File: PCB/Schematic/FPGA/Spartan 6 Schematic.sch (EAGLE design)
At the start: 28 parts, among them IC1 XC6SLX25-FT256

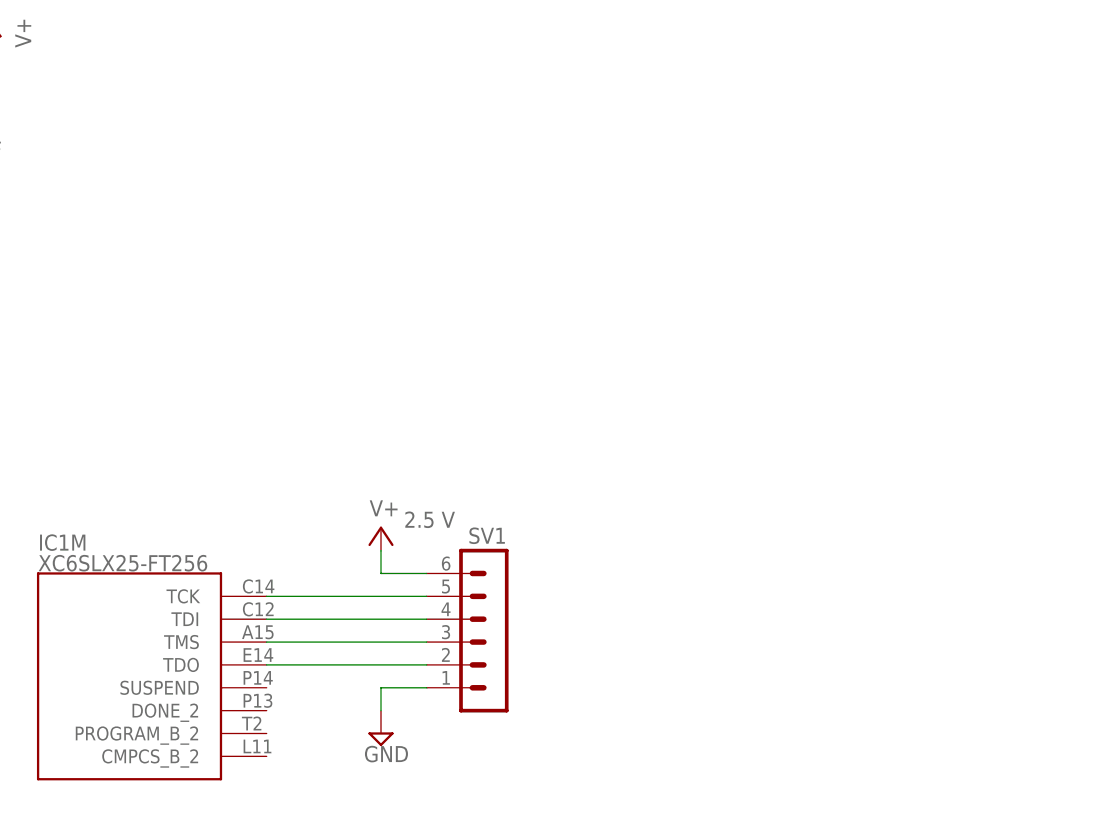
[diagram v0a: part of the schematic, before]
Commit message: FPGA MUX addition
Updated FPGA schematic to include multiplexer for JTAG programming and
added library for Fairchild FST3257MTC multiplexer.
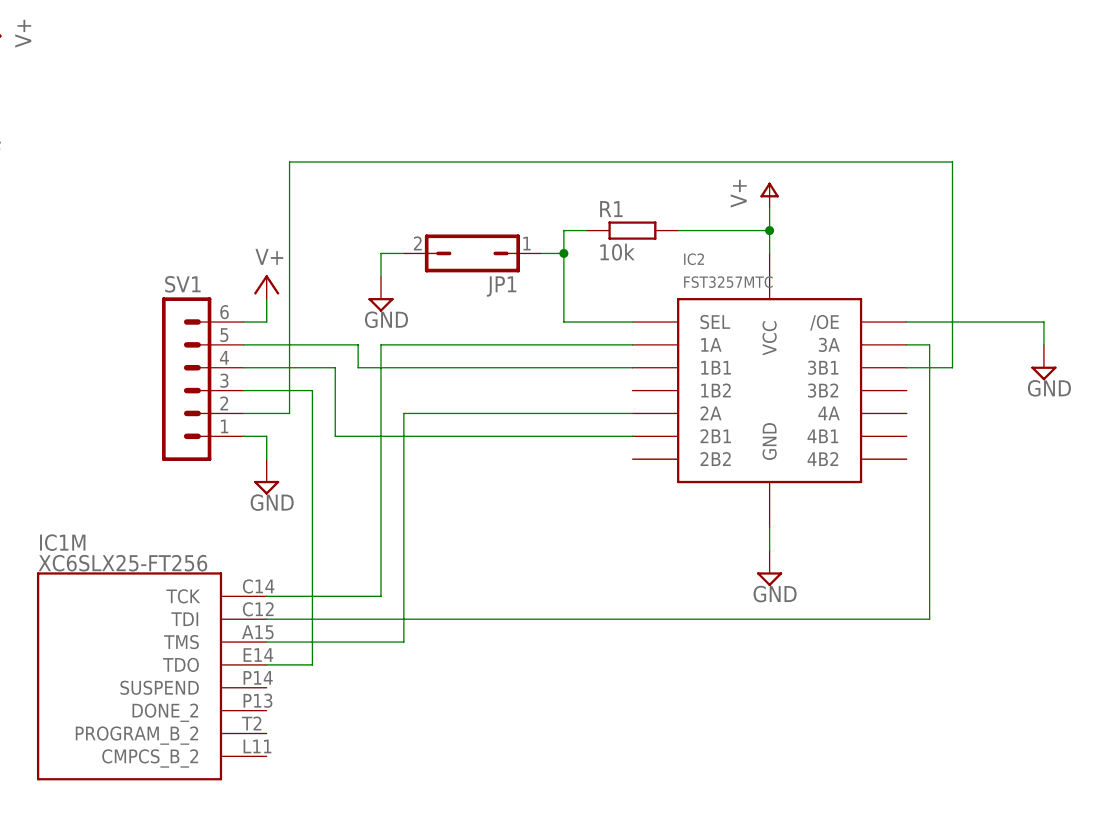
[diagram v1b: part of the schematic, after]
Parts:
- added IC2: FST3257MTC, fairchild_FST3257:FST3257MTC
- added JP1: (no value), jumper:JP1Q
- added R1: 10k, resistor:R-EU_R0805
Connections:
- new net N$5: IC1M.TCK, IC2.1A
- new net N$6: IC1M.TMS, IC2.2A
- new net N$7: IC1M.TDI, IC2.3A
- new net N$8: IC2.SEL, JP1.1, R1.1
- net GND: now also IC2./OE, IC2.GND, JP1.2
- net N$1: now also IC2.1B1; no longer IC1M.TCK
- net N$2: now also IC2.2B1; no longer IC1M.TDI
- net N$3: now also IC1M.TDO; no longer IC1M.TMS
- net N$4: now also IC2.3B1; no longer IC1M.TDO
- net VCCIO_2: now also IC2.VCC, R1.2
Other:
- moved on the sheet: SV1
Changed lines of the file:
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@@
 <part name="P+6" library="supply1" deviceset="V+" device=""/>
 <part name="P+2" library="supply1" deviceset="V+" device=""/>
+<part name="IC2" library="fairchild_FST3257" deviceset="FST3257MTC" device=""/>
+<part name="P+7" library="supply1" deviceset="V+" device=""/>
+<part name="SUPPLY4" library="supply2" deviceset="GND" device=""/>
+<part name="SUPPLY6" library="supply2" deviceset="GND" device=""/>
+<part name="JP1" library="jumper" deviceset="JP1Q" device=""/>
+<part name="R1" library="resistor" deviceset="R-EU_" device="R0805" value="10k"/>
+<part name="SUPPLY9" library="supply2" deviceset="GND" device=""/>
 </parts>
 <sheets>
@@
 <instance part="C26" gate="G$1" x="381" y="96.52"/>
 <instance part="SUPPLY13" gate="GND" x="381" y="88.9"/>
-<instance part="SV1" gate="1" x="474.98" y="17.78" rot="MR0"/>
-<instance part="SUPPLY3" gate="GND" x="462.28" y="5.08"/>
-<instance part="VCCAUX1" gate="1" x="462.28" y="27.94">
-<attribute name="VCCO" x="464.82" y="27.94" size="1.778" layer="96"/>
-</instance>
+<instance part="SV1" gate="1" x="439.42" y="45.72"/>
+<instance part="SUPPLY3" gate="GND" x="449.58" y="33.02"/>
+<instance part="VCCAUX1" gate="1" x="449.58" y="55.88"/>
 <instance part="P+1" gate="1" x="391.16" y="101.6" rot="MR0"/>
 <instance part="P+3" gate="1" x="391.16" y="60.96" rot="MR0"/>
@@
 <instance part="P+6" gate="1" x="391.16" y="15.24" rot="MR0"/>
 <instance part="P+2" gate="1" x="419.1" y="83.82" rot="MR0"/>
+<instance part="IC2" gate="G$1" x="505.46" y="43.18"/>
+<instance part="P+7" gate="1" x="505.46" y="66.04"/>
+<instance part="SUPPLY4" gate="GND" x="505.46" y="22.86"/>
+<instance part="SUPPLY6" gate="GND" x="535.94" y="45.72"/>
+<instance part="JP1" gate="A" x="472.44" y="58.42" rot="R90"/>
+<instance part="R1" gate="G$1" x="490.22" y="60.96"/>
+<instance part="SUPPLY9" gate="GND" x="462.28" y="53.34"/>
 </instances>
 <busses>
@@
 <segment>
 <pinref part="SV1" gate="1" pin="1"/>
-<wire x1="467.36" y1="10.16" x2="462.28" y2="10.16" width="0.1524" layer="91"/>
-<wire x1="462.28" y1="10.16" x2="462.28" y2="7.62" width="0.1524" layer="91"/>
+<wire x1="447.04" y1="38.1" x2="449.58" y2="38.1" width="0.1524" layer="91"/>
+<wire x1="449.58" y1="38.1" x2="449.58" y2="35.56" width="0.1524" layer="91"/>
 <pinref part="SUPPLY3" gate="GND" pin="GND"/>
+</segment>
+<segment>
+<pinref part="SUPPLY4" gate="GND" pin="GND"/>
+<pinref part="IC2" gate="G$1" pin="GND"/>
+<wire x1="505.46" y1="25.4" x2="505.46" y2="27.94" width="0.1524" layer="91"/>
+</segment>
+<segment>
+<pinref part="IC2" gate="G$1" pin="/OE"/>
+<pinref part="SUPPLY6" gate="GND" pin="GND"/>
+<wire x1="520.7" y1="50.8" x2="535.94" y2="50.8" width="0.1524" layer="91"/>
+<wire x1="535.94" y1="50.8" x2="535.94" y2="48.26" width="0.1524" layer="91"/>
+</segment>
+<segment>
+<pinref part="SUPPLY9" gate="GND" pin="GND"/>
+<pinref part="JP1" gate="A" pin="2"/>
+<wire x1="462.28" y1="55.88" x2="462.28" y2="58.42" width="0.1524" layer="91"/>
+<wire x1="462.28" y1="58.42" x2="464.82" y2="58.42" width="0.1524" layer="91"/>
 </segment>
 </net>
@@
 <pinref part="VCCAUX1" gate="1" pin="V+"/>
 <pinref part="SV1" gate="1" pin="6"/>
-<wire x1="462.28" y1="25.4" x2="462.28" y2="22.86" width="0.1524" layer="91"/>
-<wire x1="462.28" y1="22.86" x2="467.36" y2="22.86" width="0.1524" layer="91"/>
-</segment>
-</net>
-<net name="N$1" class="0">
-<segment>
-<pinref part="IC1" gate="M" pin="TCK"/>
-<pinref part="SV1" gate="1" pin="5"/>
-<wire x1="449.58" y1="20.32" x2="467.36" y2="20.32" width="0.1524" layer="91"/>
-</segment>
-</net>
-<net name="N$2" class="0">
-<segment>
-<pinref part="IC1" gate="M" pin="TDI"/>
-<pinref part="SV1" gate="1" pin="4"/>
-<wire x1="449.58" y1="17.78" x2="467.36" y2="17.78" width="0.1524" layer="91"/>
-</segment>
-</net>
-<net name="N$3" class="0">
-<segment>
-<pinref part="IC1" gate="M" pin="TMS"/>
-<pinref part="SV1" gate="1" pin="3"/>
-<wire x1="449.58" y1="15.24" x2="467.36" y2="15.24" width="0.1524" layer="91"/>
-</segment>
-</net>
-<net name="N$4" class="0">
-<segment>
-<pinref part="IC1" gate="M" pin="TDO"/>
-<pinref part="SV1" gate="1" pin="2"/>
-<wire x1="449.58" y1="12.7" x2="467.36" y2="12.7" width="0.1524" layer="91"/>
+<wire x1="449.58" y1="53.34" x2="449.58" y2="50.8" width="0.1524" layer="91"/>
+<wire x1="449.58" y1="50.8" x2="447.04" y2="50.8" width="0.1524" layer="91"/>
 </segment>
 </net>
@@
 <junction x="327.66" y="25.4"/>
 </segment>
+<segment>
+<pinref part="IC2" gate="G$1" pin="VCC"/>
+<pinref part="P+7" gate="1" pin="V+"/>
+<wire x1="505.46" y1="58.42" x2="505.46" y2="60.96" width="0.1524" layer="91"/>
+<pinref part="R1" gate="G$1" pin="2"/>
+<wire x1="505.46" y1="60.96" x2="505.46" y2="63.5" width="0.1524" layer="91"/>
+<wire x1="495.3" y1="60.96" x2="505.46" y2="60.96" width="0.1524" layer="91"/>
+<junction x="505.46" y="60.96"/>
+</segment>
 </net>
 <net name="VCCIO_3" class="0">
@@
 </segment>
 </net>
+<net name="N$1" class="0">
+<segment>
+<pinref part="SV1" gate="1" pin="5"/>
+<wire x1="447.04" y1="48.26" x2="459.74" y2="48.26" width="0.1524" layer="91"/>
+<wire x1="459.74" y1="48.26" x2="459.74" y2="45.72" width="0.1524" layer="91"/>
+<pinref part="IC2" gate="G$1" pin="1B1"/>
+<wire x1="459.74" y1="45.72" x2="490.22" y2="45.72" width="0.1524" layer="91"/>
+</segment>
+</net>
+<net name="N$2" class="0">
+<segment>
+<pinref part="SV1" gate="1" pin="4"/>
+<wire x1="447.04" y1="45.72" x2="457.2" y2="45.72" width="0.1524" layer="91"/>
+<wire x1="457.2" y1="45.72" x2="457.2" y2="38.1" width="0.1524" layer="91"/>
+<pinref part="IC2" gate="G$1" pin="2B1"/>
+<wire x1="457.2" y1="38.1" x2="490.22" y2="38.1" width="0.1524" layer="91"/>
+</segment>
+</net>
+<net name="N$3" class="0">
+<segment>
+<pinref part="SV1" gate="1" pin="3"/>
+<wire x1="447.04" y1="43.18" x2="454.66" y2="43.18" width="0.1524" layer="91"/>
+<pinref part="IC1" gate="M" pin="TDO"/>
+<wire x1="454.66" y1="43.18" x2="454.66" y2="12.7" width="0.1524" layer="91"/>
+<wire x1="454.66" y1="12.7" x2="449.58" y2="12.7" width="0.1524" layer="91"/>
+</segment>
+</net>
+<net name="N$4" class="0">
+<segment>
+<pinref part="SV1" gate="1" pin="2"/>
+<wire x1="447.04" y1="40.64" x2="452.12" y2="40.64" width="0.1524" layer="91"/>
+<wire x1="452.12" y1="68.58" x2="525.78" y2="68.58" width="0.1524" layer="91"/>
+<pinref part="IC2" gate="G$1" pin="3B1"/>
+<wire x1="525.78" y1="68.58" x2="525.78" y2="45.72" width="0.1524" layer="91"/>
+<wire x1="525.78" y1="45.72" x2="520.7" y2="45.72" width="0.1524" layer="91"/>
+<wire x1="452.12" y1="40.64" x2="452.12" y2="68.58" width="0.1524" layer="91"/>
+</segment>
+</net>
+<net name="N$5" class="0">
+<segment>
+<pinref part="IC2" gate="G$1" pin="1A"/>
+<wire x1="490.22" y1="48.26" x2="462.28" y2="48.26" width="0.1524" layer="91"/>
+<pinref part="IC1" gate="M" pin="TCK"/>
+<wire x1="462.28" y1="48.26" x2="462.28" y2="20.32" width="0.1524" layer="91"/>
+<wire x1="462.28" y1="20.32" x2="449.58" y2="20.32" width="0.1524" layer="91"/>
+</segment>
+</net>
+<net name="N$6" class="0">
+<segment>
+<pinref part="IC2" gate="G$1" pin="2A"/>
+<wire x1="490.22" y1="40.64" x2="464.82" y2="40.64" width="0.1524" layer="91"/>
+<pinref part="IC1" gate="M" pin="TMS"/>
+<wire x1="464.82" y1="40.64" x2="464.82" y2="15.24" width="0.1524" layer="91"/>
+<wire x1="464.82" y1="15.24" x2="449.58" y2="15.24" width="0.1524" layer="91"/>
+</segment>
+</net>
+<net name="N$7" class="0">
+<segment>
+<pinref part="IC2" gate="G$1" pin="3A"/>
+<wire x1="520.7" y1="48.26" x2="523.24" y2="48.26" width="0.1524" layer="91"/>
+<pinref part="IC1" gate="M" pin="TDI"/>
+<wire x1="523.24" y1="48.26" x2="523.24" y2="17.78" width="0.1524" layer="91"/>
+<wire x1="523.24" y1="17.78" x2="449.58" y2="17.78" width="0.1524" layer="91"/>
+</segment>
+</net>
+<net name="N$8" class="0">
+<segment>
+<pinref part="IC2" gate="G$1" pin="SEL"/>
+<pinref part="R1" gate="G$1" pin="1"/>
+<wire x1="490.22" y1="50.8" x2="482.6" y2="50.8" width="0.1524" layer="91"/>
+<wire x1="482.6" y1="50.8" x2="482.6" y2="58.42" width="0.1524" layer="91"/>
+<pinref part="JP1" gate="A" pin="1"/>
+<wire x1="482.6" y1="58.42" x2="482.6" y2="60.96" width="0.1524" layer="91"/>
+<wire x1="482.6" y1="60.96" x2="485.14" y2="60.96" width="0.1524" layer="91"/>
+<wire x1="482.6" y1="58.42" x2="480.06" y2="58.42" width="0.1524" layer="91"/>
+<junction x="482.6" y="58.42"/>
+</segment>
+</net>
